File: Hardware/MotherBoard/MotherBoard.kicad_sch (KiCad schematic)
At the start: 20 parts, among them J1 POWER, J10 I/O_PWR, J2 I/O0, J3 ISA00, J4 ISA10, J5 I/O1, J6 EXTRN_CLCK, J7 ISA01, J8 ISA11, U1 AMS1117-5.0

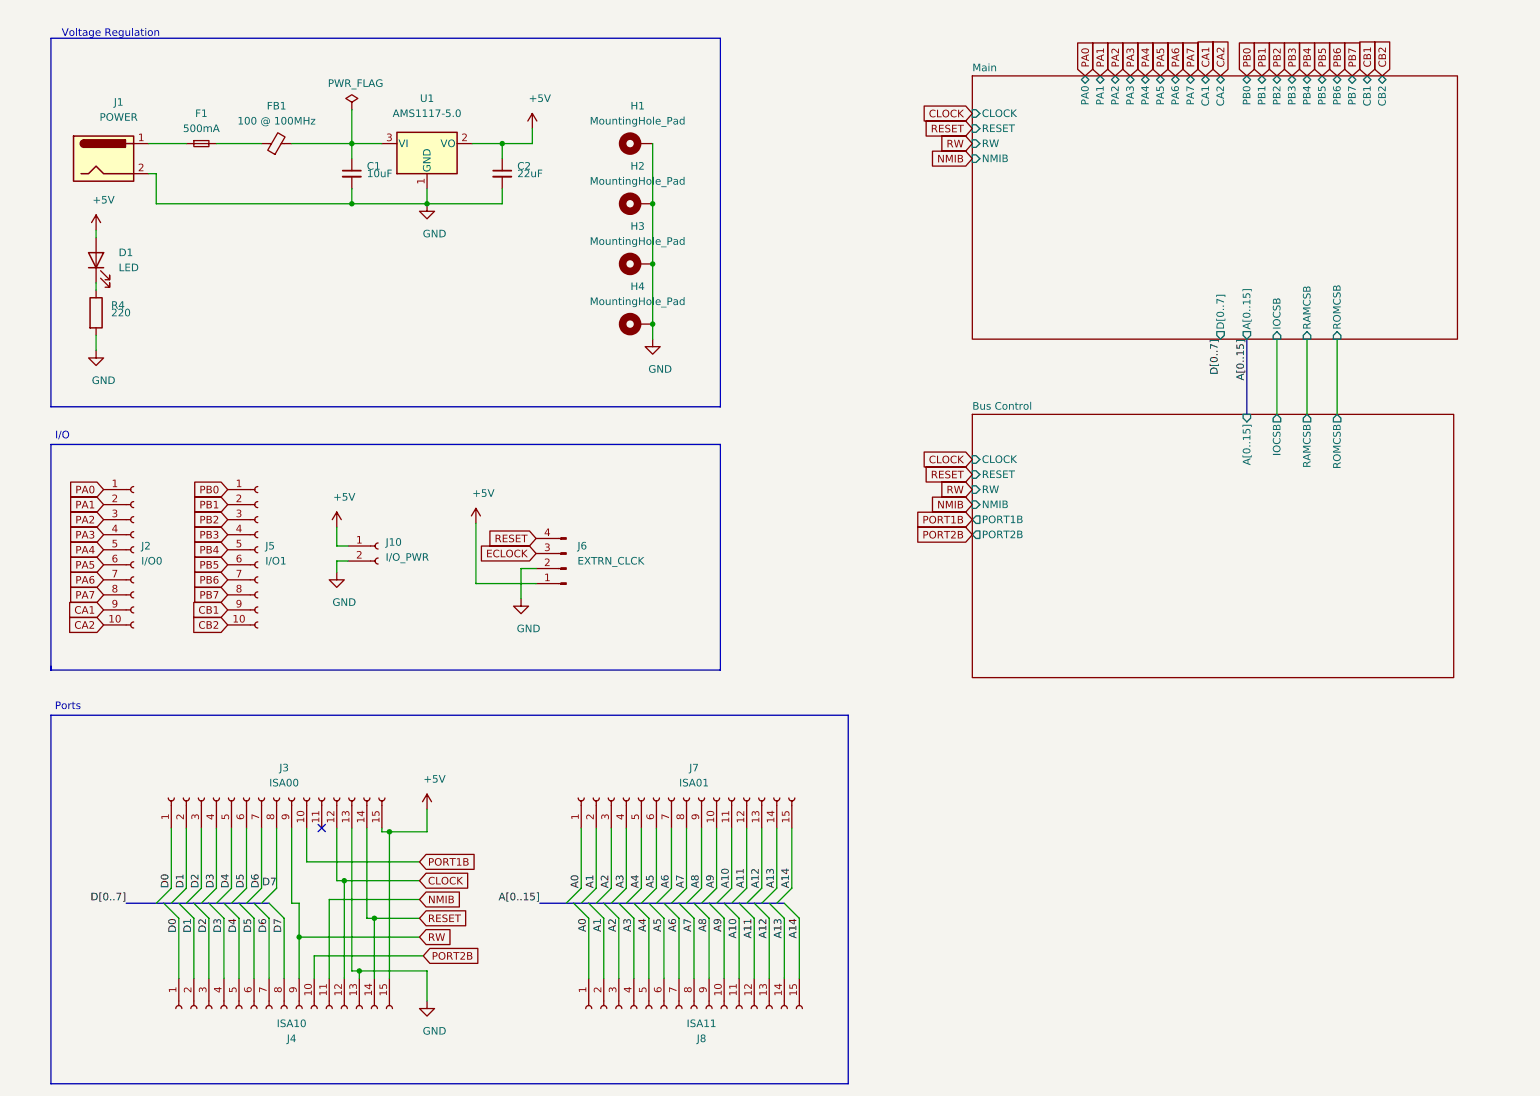
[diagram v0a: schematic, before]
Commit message: Add buffers to extenstion ports
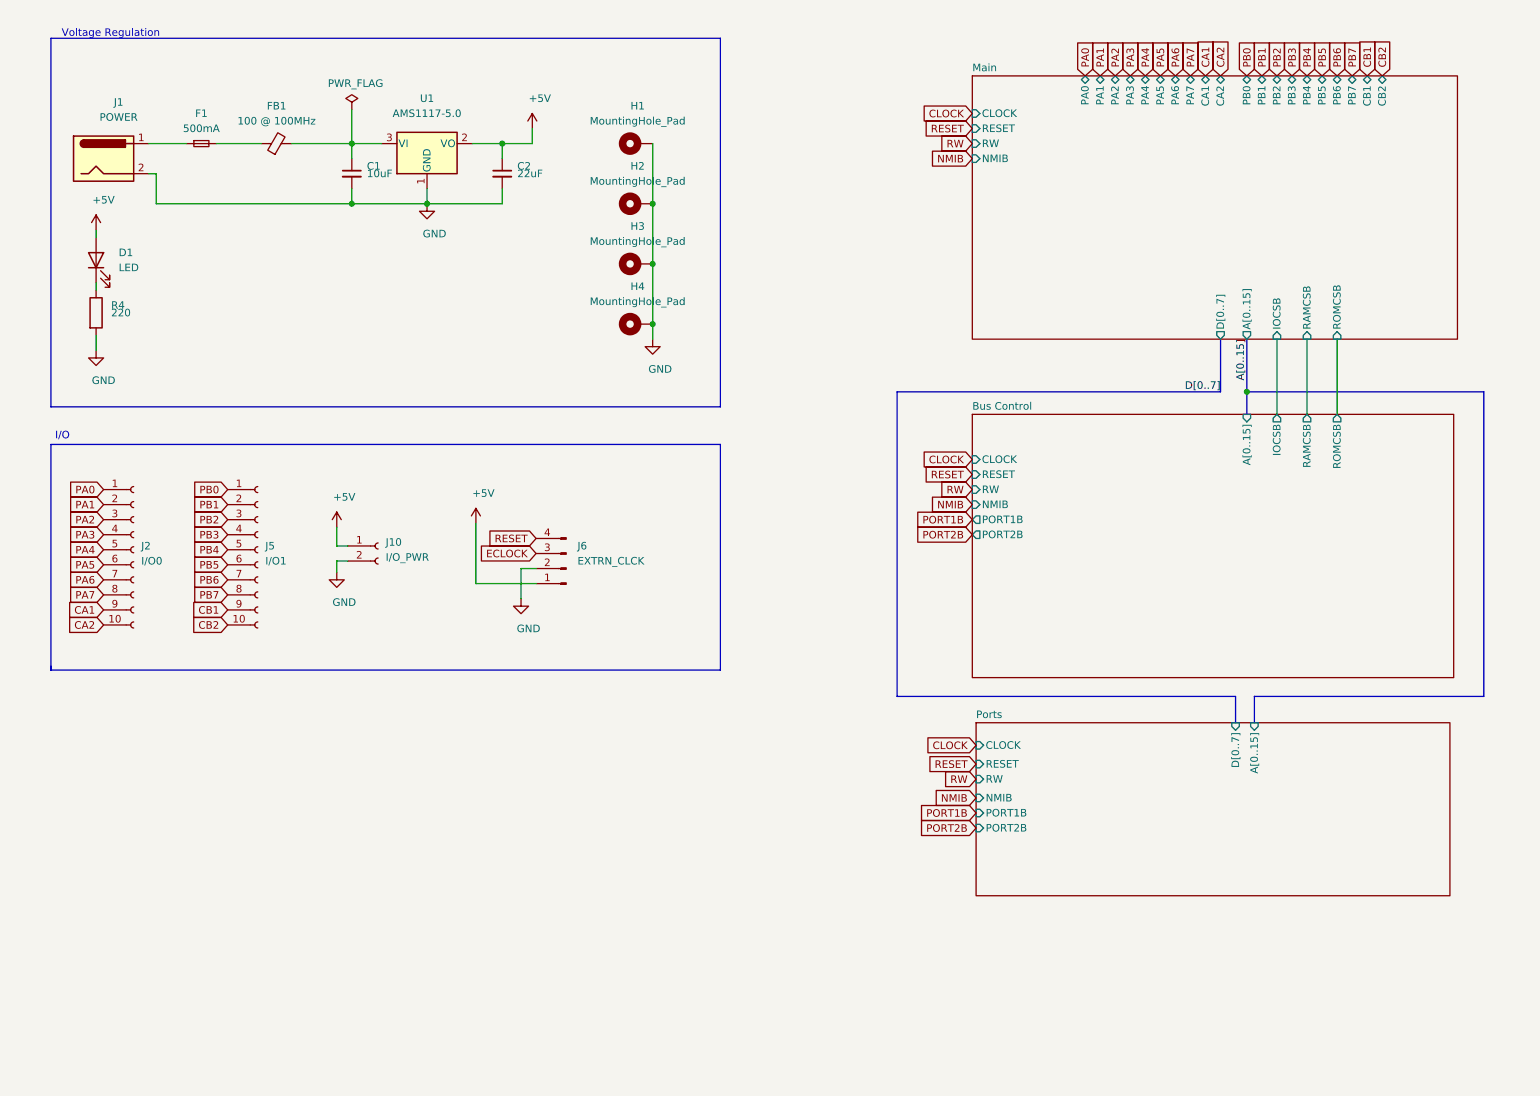
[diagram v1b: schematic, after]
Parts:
- removed J3: ISA00, Connector_PinSocket_2.54mm:PinSocket_1x15_P2.54mm_Vertical, symbol Connector:Conn_01x15_Female
- removed J4: ISA10, Connector_PinSocket_2.54mm:PinSocket_1x15_P2.54mm_Vertical, symbol Connector:Conn_01x15_Female
- removed J7: ISA01, Connector_PinSocket_2.54mm:PinSocket_1x15_P2.54mm_Vertical, symbol Connector:Conn_01x15_Female
- removed J8: ISA11, Connector_PinSocket_2.54mm:PinSocket_1x15_P2.54mm_Vertical, symbol Connector:Conn_01x15_Female
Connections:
- no-connect marks 1 -> 0
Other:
- added sheet Ports (BusExtentions.kicad_sch)
- sheet Bus Control: file /home/romuald/Projects/KiCad/Retro6502/BusControl.kicad_sch -> /home/romuald/Projects/Miniish/Hardware/MotherBoard/BusControl.kicad_sch
- sheet Main: file /home/romuald/Projects/KiCad/Retro6502/Main.kicad_sch -> /home/romuald/Projects/Miniish/Hardware/MotherBoard/Main.kicad_sch
- note removed: "Ports"

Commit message: Fix
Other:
- sheet Main renamed CPU 
- sheet Bus Control ports: added none; removed NMIB, RESET, RW
- sheet CPU  ports: added ECLOCK; removed none
- moved on the sheet: C1, C2, D1, F1, FB1, H1, H2, H3, H4, J1, J10, J2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

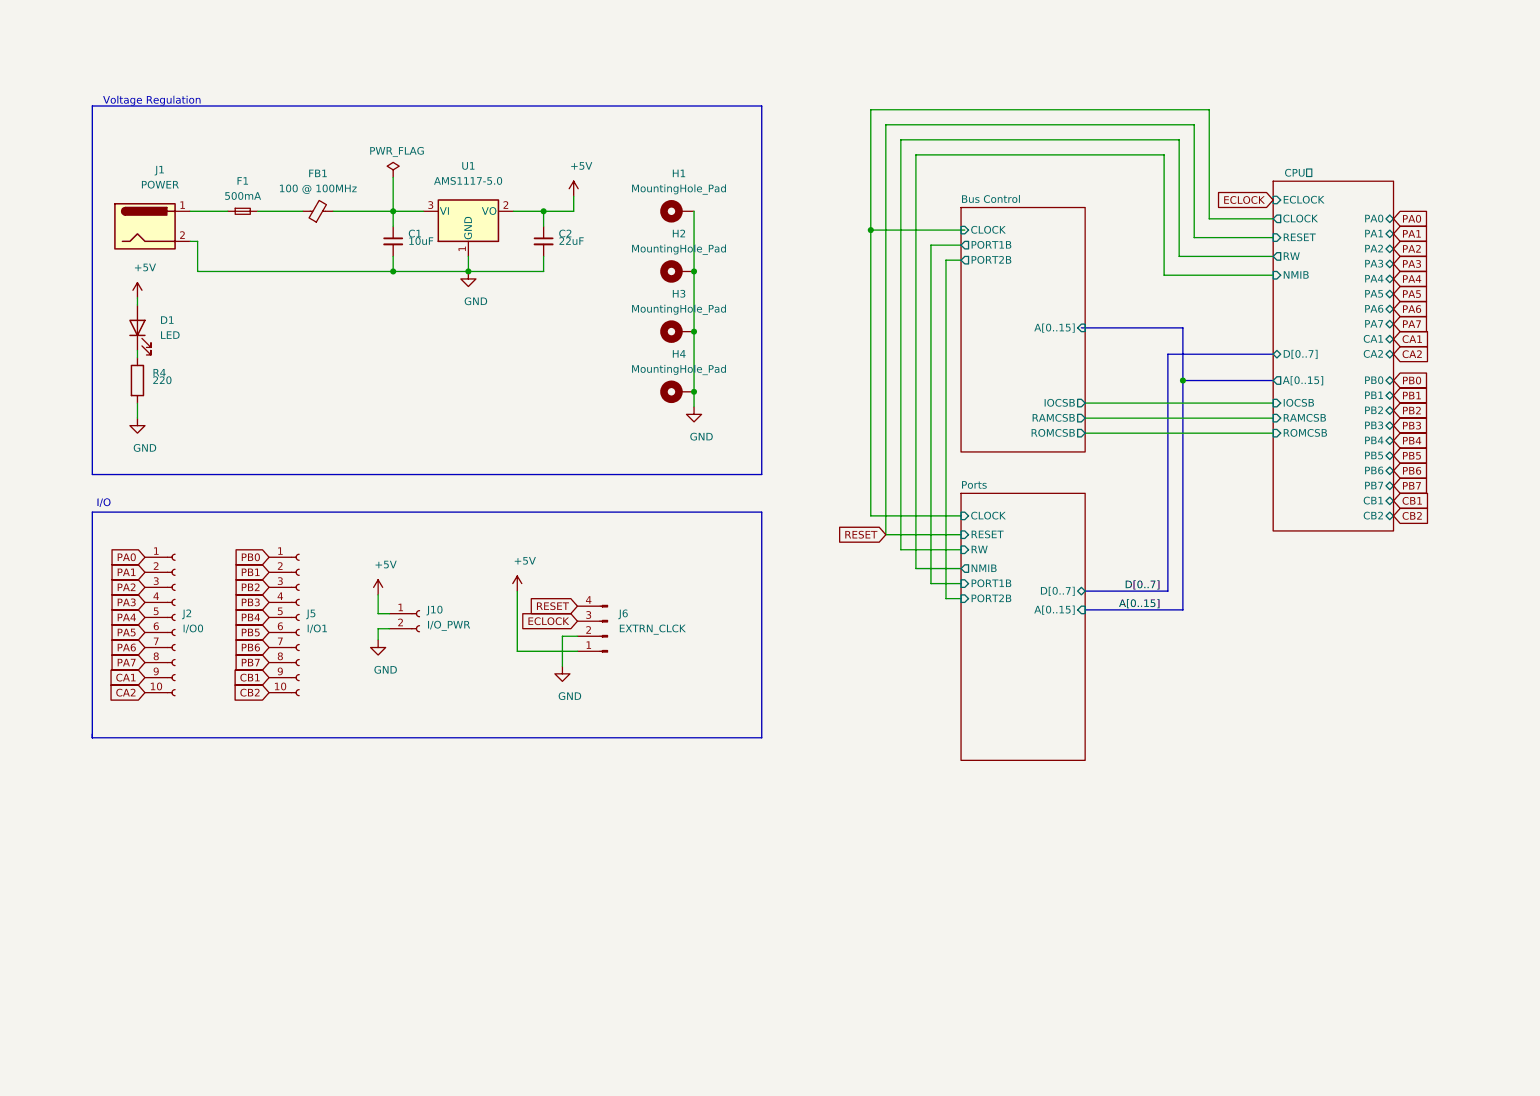
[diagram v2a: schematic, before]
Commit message: Replace logic IC 4xxx by 74hcxx
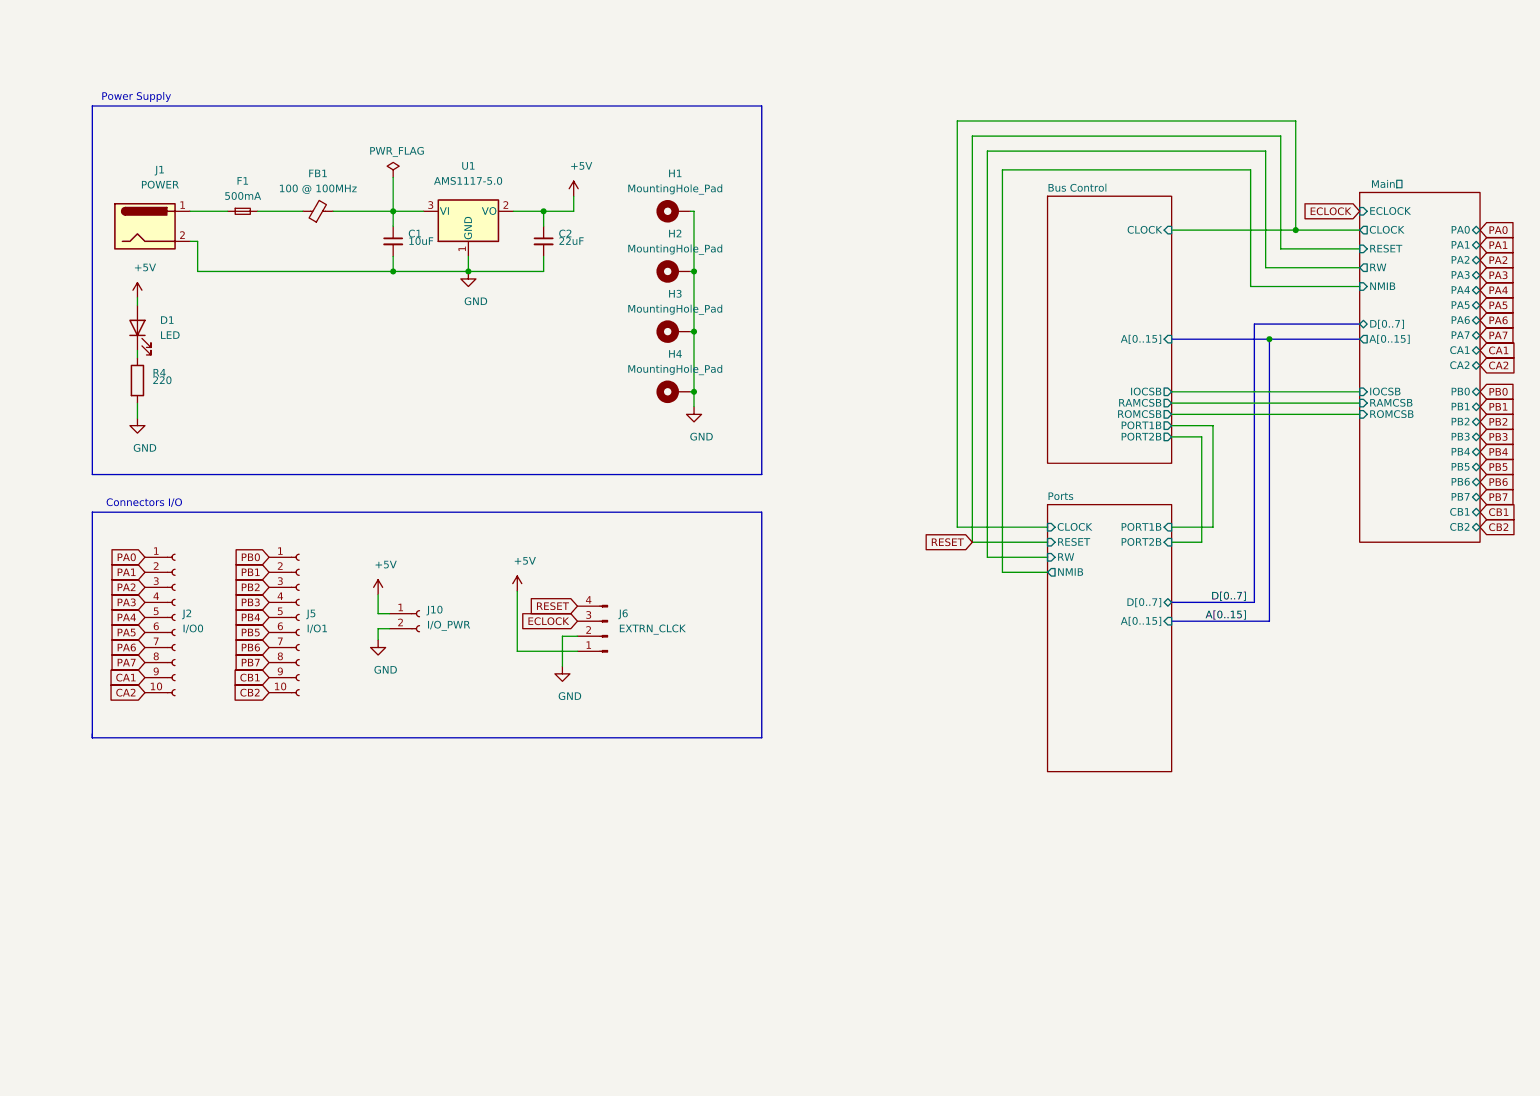
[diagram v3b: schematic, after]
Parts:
- U1: footprint Package_TO_SOT_THT:TO-220-3_Horizontal_TabDown -> Package_TO_SOT_SMD:SOT-223-3_TabPin2
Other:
- sheet CPU  renamed Main 
- note added: "Connectors I/O"
- note added: "Power Supply"
- note removed: "I/O"
- note removed: "Voltage Regulation"
- moved on the sheet: H1, H2, H3, H4

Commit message: Finalize daughter board
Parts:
- C1, C2: symbol Device:C_Small -> Device:CP_Small
- U1: footprint Package_TO_SOT_SMD:SOT-223-3_TabPin2 -> Package_TO_SOT_THT:TO-220-3_Horizontal_TabDown

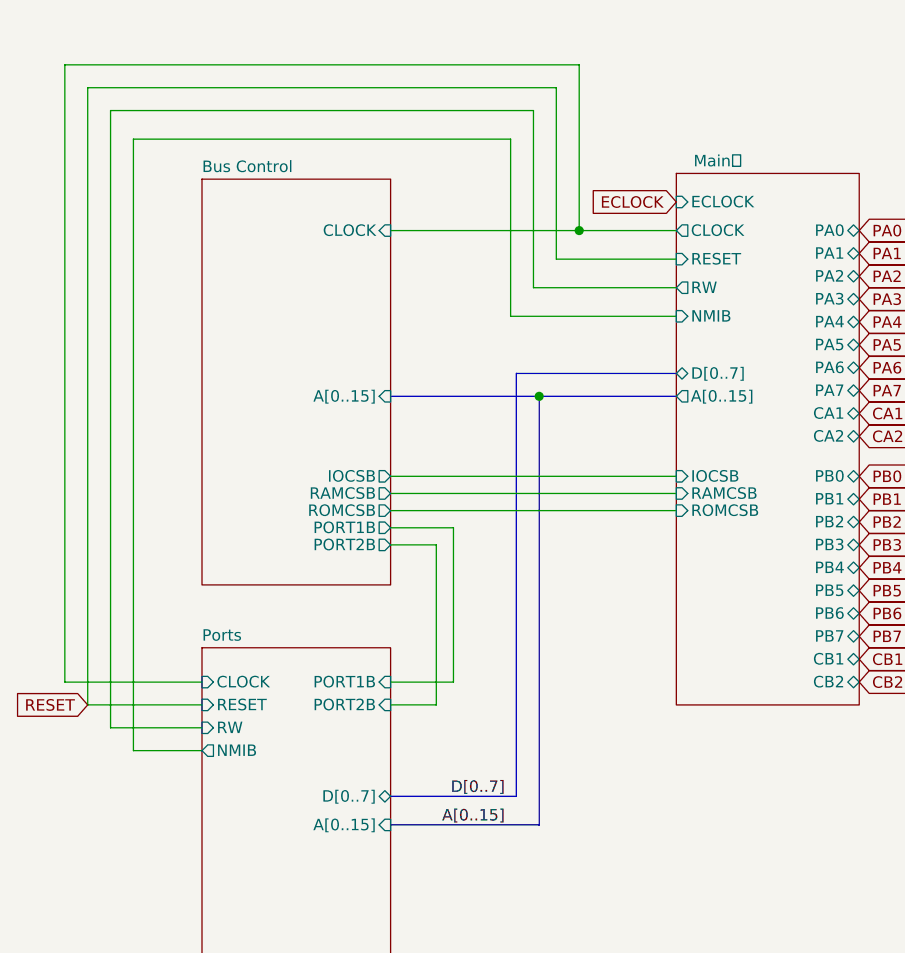
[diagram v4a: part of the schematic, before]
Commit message: Implement APU and fix schematics
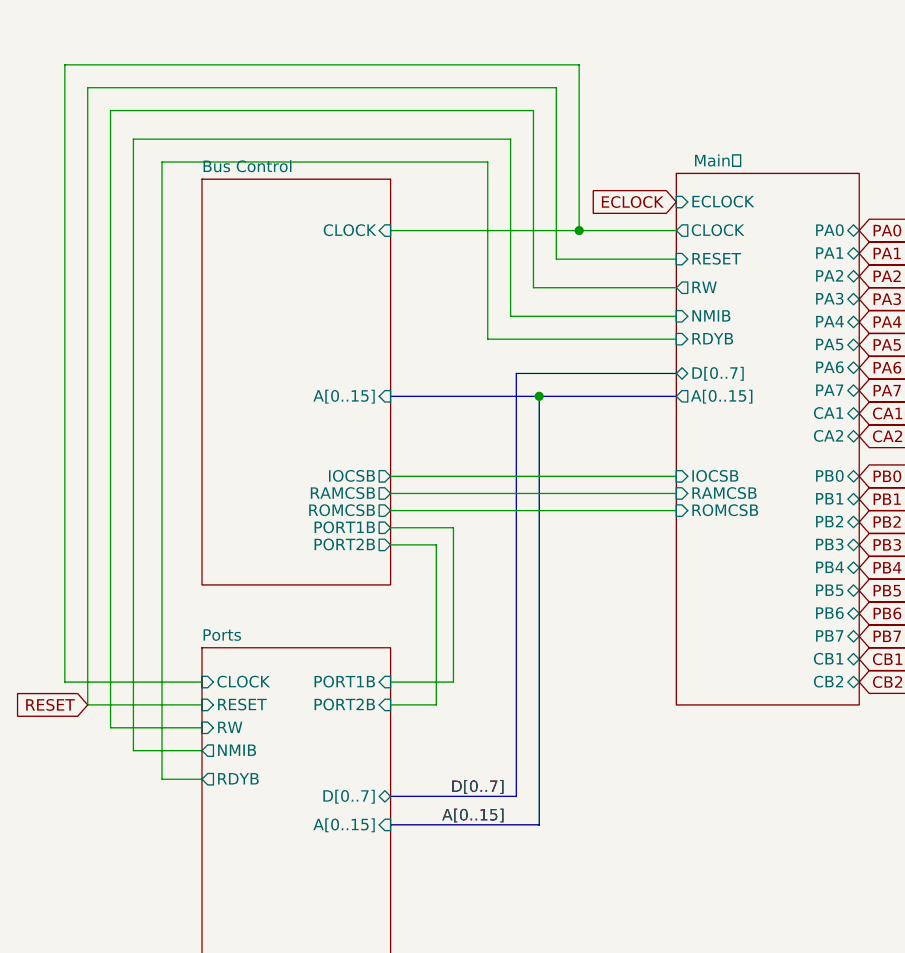
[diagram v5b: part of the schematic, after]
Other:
- sheet Main  ports: added RDYB; removed none
- sheet Ports ports: added RDYB; removed none
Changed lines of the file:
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@@
     (company "Romuald Rousseau")
   )
+  (bus_alias "A11" (members "A11"))
   (bus_alias "A12" (members "A12"))
-  (bus_alias "A11" (members "A11"))
   (junction (at 76.835 47.625) (diameter 1.016) (color 0 0 0 0))
   (junction (at 76.835 57.785) (diameter 1.016) (color 0 0 0 0))
@@
     (stroke (width 0) (type solid) (color 0 0 0 0))
   )
+  (wire (pts (xy 182.88 43.18) (xy 182.88 111.76))
+    (stroke (width 0) (type solid) (color 0 0 0 0))
+  )
+  (wire (pts (xy 182.88 111.76) (xy 187.325 111.76))
+    (stroke (width 0) (type solid) (color 0 0 0 0))
+  )
   (wire (pts (xy 208.28 50.8) (xy 229.235 50.8))
     (stroke (width 0) (type solid) (color 0 0 0 0))
@@
     (stroke (width 0) (type solid) (color 0 0 0 0))
   )
+  (wire (pts (xy 219.075 43.18) (xy 182.88 43.18))
+    (stroke (width 0) (type solid) (color 0 0 0 0))
+  )
+  (wire (pts (xy 219.075 62.865) (xy 219.075 43.18))
+    (stroke (width 0) (type solid) (color 0 0 0 0))
+  )
   (wire (pts (xy 221.615 40.64) (xy 179.705 40.64))
     (stroke (width 0) (type solid) (color 0 0 0 0))
@@
   )
   (wire (pts (xy 240.03 60.325) (xy 221.615 60.325))
+    (stroke (width 0) (type solid) (color 0 0 0 0))
+  )
+  (wire (pts (xy 240.03 62.865) (xy 219.075 62.865))
     (stroke (width 0) (type solid) (color 0 0 0 0))
   )
@@
       (effects (font (size 1.27 1.27)) (justify left))
     )
+    (pin "RDYB" input (at 240.03 62.865 180)
+      (effects (font (size 1.27 1.27)) (justify left))
+    )
   )
   (sheet (at 187.325 97.155) (size 20.955 45.085)
@@
       (effects (font (size 1.27 1.27)) (justify left))
     )
+    (pin "RDYB" output (at 187.325 111.76 180)
+      (effects (font (size 1.27 1.27)) (justify left))
+    )
   )
   (sheet_instances
@@
     )
     (path "/6cbd16f3-a1f6-4857-8623-5a6775377a9a/a33e05e8-4a0b-4de9-82f3-216a64ed2403"
-      (reference "J3") (unit 1) (value "ISA00") (footprint "Connector_PinSocket_2.54mm:PinSocket_1x15_P2.54mm_Vertical")
+      (reference "J3") (unit 1) (value "ISA00") (footprint "Connector_PinSocket_2.54mm:PinSocket_1x16_P2.54mm_Vertical")
     )
     (path "/6cbd16f3-a1f6-4857-8623-5a6775377a9a/ad97b31a-c5ce-4faa-a2d0-e001fa0cc350"
-      (reference "J4") (unit 1) (value "ISA10") (footprint "Connector_PinSocket_2.54mm:PinSocket_1x15_P2.54mm_Vertical")
+      (reference "J4") (unit 1) (value "ISA10") (footprint "Connector_PinSocket_2.54mm:PinSocket_1x16_P2.54mm_Vertical")
     )
     (path "/6cbd16f3-a1f6-4857-8623-5a6775377a9a/fa838b97-f421-46fa-ac1e-9a2f6ddd7e0c"
-      (reference "J7") (unit 1) (value "ISA01") (footprint "Connector_PinSocket_2.54mm:PinSocket_1x15_P2.54mm_Vertical")
+      (reference "J7") (unit 1) (value "ISA01") (footprint "Connector_PinSocket_2.54mm:PinSocket_1x16_P2.54mm_Vertical")
     )
     (path "/6cbd16f3-a1f6-4857-8623-5a6775377a9a/19cc7f8e-7a0d-4fe2-9625-721aeb7bd93d"
-      (reference "J8") (unit 1) (value "ISA11") (footprint "Connector_PinSocket_2.54mm:PinSocket_1x15_P2.54mm_Vertical")
+      (reference "J8") (unit 1) (value "ISA11") (footprint "Connector_PinSocket_2.54mm:PinSocket_1x16_P2.54mm_Vertical")
     )
     (path "/6cbd16f3-a1f6-4857-8623-5a6775377a9a/1e640dc0-9a9b-4e78-97a7-c4c4fba75621"
